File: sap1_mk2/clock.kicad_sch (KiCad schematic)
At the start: 28 parts, among them SW1 SW_Push, SW2 SW_SPDT, U1 NE555P, U2 NE555P, U3 NE555P, U4 74LS04, U5 74LS08, U6 74LS32

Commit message: assigned footprints + finished root schematic
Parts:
- C1: footprint (none) -> Capacitor_THT:CP_Radial_D4.0mm_P2.00mm
- C10, C11, C2, C3, C4, C5, C6, C7, C8, C9: footprint (none) -> Capacitor_THT:C_Disc_D5.0mm_W2.5mm_P2.50mm
- D1: footprint (none) -> LED_THT:LED_D3.0mm
- R1, R2, R3, R4, R5, R6, R7: footprint (none) -> Resistor_THT:R_Axial_DIN0207_L6.3mm_D2.5mm_P10.16mm_Horizontal
- RV1: footprint (none) -> Potentiometer_THT:Potentiometer_Bourns_3296W_Vertical
- SW1: footprint (none) -> Button_Switch_THT:SW_PUSH-12mm
- SW2: footprint (none) -> Button_Switch_THT:SW_Push_2P2T_Toggle_CK_PVA2OAH5xxxxxxV2
- U4, U5, U6: footprint (none) -> Package_DIP:DIP-14_W7.62mm
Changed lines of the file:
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@@
 			)
 		)
-		(property "Footprint" ""
+		(property "Footprint" "Capacitor_THT:C_Disc_D5.0mm_W2.5mm_P2.50mm"
 			(at 17.78 177.8 0)
 			(hide yes)
@@
 			)
 		)
-		(property "Footprint" ""
+		(property "Footprint" "Package_DIP:DIP-14_W7.62mm"
 			(at 130.81 177.8 0)
 			(hide yes)
@@
 			)
 		)
-		(property "Footprint" ""
+		(property "Footprint" "Package_DIP:DIP-14_W7.62mm"
 			(at 168.91 99.06 0)
 			(hide yes)
@@
 			)
 		)
-		(property "Footprint" ""
+		(property "Footprint" "Capacitor_THT:C_Disc_D5.0mm_W2.5mm_P2.50mm"
 			(at 36.83 50.8 0)
 			(hide yes)
@@
 			)
 		)
-		(property "Footprint" ""
+		(property "Footprint" "Package_DIP:DIP-14_W7.62mm"
 			(at 256.54 101.6 0)
 			(hide yes)
@@
 			)
 		)
-		(property "Footprint" ""
+		(property "Footprint" "Package_DIP:DIP-14_W7.62mm"
 			(at 168.91 118.11 0)
 			(hide yes)
@@
 			)
 		)
-		(property "Footprint" ""
+		(property "Footprint" "Package_DIP:DIP-14_W7.62mm"
 			(at 48.26 177.8 0)
 			(hide yes)
@@
 			)
 		)
-		(property "Footprint" ""
+		(property "Footprint" "Resistor_THT:R_Axial_DIN0207_L6.3mm_D2.5mm_P10.16mm_Horizontal"
 			(at 236.982 130.81 90)
 			(hide yes)
@@
 			)
 		)
-		(property "Footprint" ""
+		(property "Footprint" "Capacitor_THT:C_Disc_D5.0mm_W2.5mm_P2.50mm"
 			(at 64.77 177.8 0)
 			(hide yes)
@@
 			)
 		)
-		(property "Footprint" ""
+		(property "Footprint" "Capacitor_THT:C_Disc_D5.0mm_W2.5mm_P2.50mm"
 			(at 168.91 66.04 0)
 			(hide yes)
@@
 			)
 		)
-		(property "Footprint" ""
+		(property "Footprint" "Package_DIP:DIP-14_W7.62mm"
 			(at 194.31 109.22 0)
 			(hide yes)
@@
 			)
 		)
-		(property "Footprint" ""
+		(property "Footprint" "Resistor_THT:R_Axial_DIN0207_L6.3mm_D2.5mm_P10.16mm_Horizontal"
 			(at 90.17 55.118 90)
 			(hide yes)
@@
 			)
 		)
-		(property "Footprint" ""
+		(property "Footprint" "Capacitor_THT:C_Disc_D5.0mm_W2.5mm_P2.50mm"
 			(at 44.45 68.58 0)
 			(hide yes)
@@
 			)
 		)
-		(property "Footprint" ""
+		(property "Footprint" "Package_DIP:DIP-14_W7.62mm"
 			(at 148.59 115.57 0)
 			(hide yes)
@@
 			)
 		)
-		(property "Footprint" ""
+		(property "Footprint" "Resistor_THT:R_Axial_DIN0207_L6.3mm_D2.5mm_P10.16mm_Horizontal"
 			(at 167.132 35.56 90)
 			(hide yes)
@@
 			)
 		)
-		(property "Footprint" ""
+		(property "Footprint" "Resistor_THT:R_Axial_DIN0207_L6.3mm_D2.5mm_P10.16mm_Horizontal"
 			(at 206.502 38.1 90)
 			(hide yes)
@@
 			)
 		)
-		(property "Footprint" ""
+		(property "Footprint" "Resistor_THT:R_Axial_DIN0207_L6.3mm_D2.5mm_P10.16mm_Horizontal"
 			(at 131.572 38.1 90)
 			(hide yes)
@@
 			)
 		)
-		(property "Footprint" ""
+		(property "Footprint" "Capacitor_THT:C_Disc_D5.0mm_W2.5mm_P2.50mm"
 			(at 213.36 63.5 0)
 			(hide yes)
@@
 			)
 		)
-		(property "Footprint" ""
+		(property "Footprint" "Button_Switch_THT:SW_Push_2P2T_Toggle_CK_PVA2OAH5xxxxxxV2"
 			(at 203.2 53.34 0)
 			(hide yes)
@@
 			)
 		)
-		(property "Footprint" ""
+		(property "Footprint" "Potentiometer_THT:Potentiometer_Bourns_3296W_Vertical"
 			(at 99.06 53.34 0)
 			(hide yes)
@@
 			)
 		)
-		(property "Footprint" ""
+		(property "Footprint" "Package_DIP:DIP-14_W7.62mm"
 			(at 113.03 177.8 0)
 			(hide yes)
@@
 			)
 		)
-		(property "Footprint" ""
+		(property "Footprint" "Package_DIP:DIP-14_W7.62mm"
 			(at 48.26 135.89 0)
 			(hide yes)
@@
 			)
 		)
-		(property "Footprint" ""
+		(property "Footprint" "Button_Switch_THT:SW_PUSH-12mm"
 			(at 125.73 40.64 0)
 			(hide yes)
@@
 			)
 		)
-		(property "Footprint" ""
+		(property "Footprint" "Capacitor_THT:C_Disc_D5.0mm_W2.5mm_P2.50mm"
 			(at 17.78 135.89 0)
 			(hide yes)
@@
 			)
 		)
-		(property "Footprint" ""
+		(property "Footprint" "Capacitor_THT:CP_Radial_D4.0mm_P2.00mm"
 			(at 55.88 68.58 0)
 			(hide yes)
@@
 			)
 		)
-		(property "Footprint" ""
+		(property "Footprint" "Package_DIP:DIP-14_W7.62mm"
 			(at 76.2 177.8 0)
 			(hide yes)
@@
 			)
 		)
-		(property "Footprint" ""
+		(property "Footprint" "Package_DIP:DIP-14_W7.62mm"
 			(at 148.59 133.35 0)
 			(hide yes)
@@
 			)
 		)
-		(property "Footprint" ""
+		(property "Footprint" "Package_DIP:DIP-14_W7.62mm"
 			(at 81.28 135.89 0)
 			(hide yes)
@@
 			)
 		)
-		(property "Footprint" ""
+		(property "Footprint" "Capacitor_THT:C_Disc_D5.0mm_W2.5mm_P2.50mm"
 			(at 133.35 63.5 0)
 			(hide yes)
@@
 			)
 		)
-		(property "Footprint" ""
+		(property "Footprint" "Resistor_THT:R_Axial_DIN0207_L6.3mm_D2.5mm_P10.16mm_Horizontal"
 			(at 79.502 38.1 90)
 			(hide yes)
@@
 			)
 		)
-		(property "Footprint" ""
+		(property "Footprint" "LED_THT:LED_D3.0mm"
 			(at 238.76 120.65 0)
 			(hide yes)
@@
 			)
 		)
-		(property "Footprint" ""
+		(property "Footprint" "Package_DIP:DIP-14_W7.62mm"
 			(at 95.25 177.8 0)
 			(hide yes)
@@
 			)
 		)
-		(property "Footprint" ""
+		(property "Footprint" "Package_DIP:DIP-14_W7.62mm"
 			(at 222.25 111.76 0)
 			(hide yes)
@@
 			)
 		)
-		(property "Footprint" ""
+		(property "Footprint" "Package_DIP:DIP-14_W7.62mm"
 			(at 29.21 135.89 0)
 			(hide yes)
@@
 			)
 		)
-		(property "Footprint" ""
+		(property "Footprint" "Capacitor_THT:C_Disc_D5.0mm_W2.5mm_P2.50mm"
 			(at 254 50.8 0)
 			(hide yes)
@@
 			)
 		)
-		(property "Footprint" ""
+		(property "Footprint" "Package_DIP:DIP-14_W7.62mm"
 			(at 64.77 135.89 0)
 			(hide yes)
@@
 			)
 		)
-		(property "Footprint" ""
+		(property "Footprint" "Resistor_THT:R_Axial_DIN0207_L6.3mm_D2.5mm_P10.16mm_Horizontal"
 			(at 209.042 38.1 90)
 			(hide yes)
@@
 			)
 		)
-		(property "Footprint" ""
+		(property "Footprint" "Package_DIP:DIP-14_W7.62mm"
 			(at 29.21 177.8 0)
 			(hide yes)
@@
 			)
 		)
-		(property "Footprint" ""
+		(property "Footprint" "Capacitor_THT:C_Disc_D5.0mm_W2.5mm_P2.50mm"
 			(at 173.99 50.8 0)
 			(hide yes)

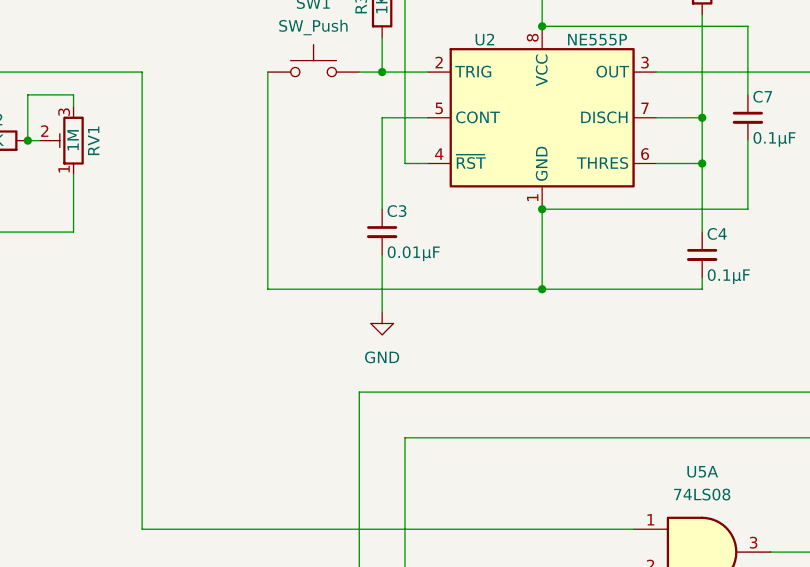
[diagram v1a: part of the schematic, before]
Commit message: placed PCB clock module
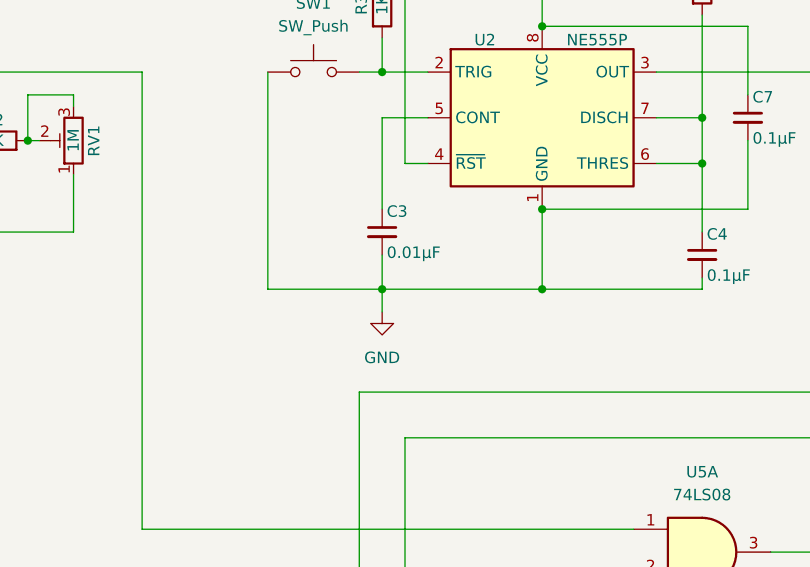
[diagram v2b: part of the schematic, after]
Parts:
- RV1: footprint Potentiometer_THT:Potentiometer_Bourns_3296W_Vertical -> Potentiometer_THT:Potentiometer_Alps_RK09L_Single_Vertical
- SW2: footprint Button_Switch_THT:SW_Push_2P2T_Toggle_CK_PVA2OAH5xxxxxxV2 -> Button_Switch_THT:SW_Slide_SPDT_Straight_CK_OS102011MS2Q
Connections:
- net GND: now also C4.2, C7.2, SW1.1, U2.1 (GND)
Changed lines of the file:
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@@
 		(color 0 0 0 0)
 	)
+	(junction
+		(at 133.35 69.85)
+		(diameter 0)
+		(color 0 0 0 0)
+	)
 	(no_connect
 		(at 64.77 128.27)
@@
 	(wire
 		(pts
-			(xy 120.65 69.85) (xy 151.13 69.85)
+			(xy 120.65 69.85) (xy 133.35 69.85)
 		)
 		(stroke
@@
 	(wire
 		(pts
-			(xy 133.35 66.04) (xy 133.35 72.39)
+			(xy 133.35 66.04) (xy 133.35 69.85)
 		)
 		(stroke
@@
 	(wire
 		(pts
+			(xy 133.35 69.85) (xy 133.35 72.39)
+		)
+		(stroke
+			(width 0)
+			(type default)
+		)
+	)
+	(wire
+		(pts
 			(xy 229.87 111.76) (xy 238.76 111.76)
 		)
@@
 	(wire
 		(pts
+			(xy 133.35 69.85) (xy 151.13 69.85)
+		)
+		(stroke
+			(width 0)
+			(type default)
+		)
+	)
+	(wire
+		(pts
 			(xy 210.82 41.91) (xy 210.82 55.88)
 		)
@@
 			)
 		)
-		(property "Footprint" "Button_Switch_THT:SW_Push_2P2T_Toggle_CK_PVA2OAH5xxxxxxV2"
+		(property "Footprint" "Button_Switch_THT:SW_Slide_SPDT_Straight_CK_OS102011MS2Q"
 			(at 203.2 53.34 0)
 			(hide yes)
@@
 			)
 		)
-		(property "Footprint" "Potentiometer_THT:Potentiometer_Bourns_3296W_Vertical"
+		(property "Footprint" "Potentiometer_THT:Potentiometer_Alps_RK09L_Single_Vertical"
 			(at 99.06 53.34 0)
 			(hide yes)
